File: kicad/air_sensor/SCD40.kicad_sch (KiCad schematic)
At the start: 10 parts, among them U7 ATtiny412

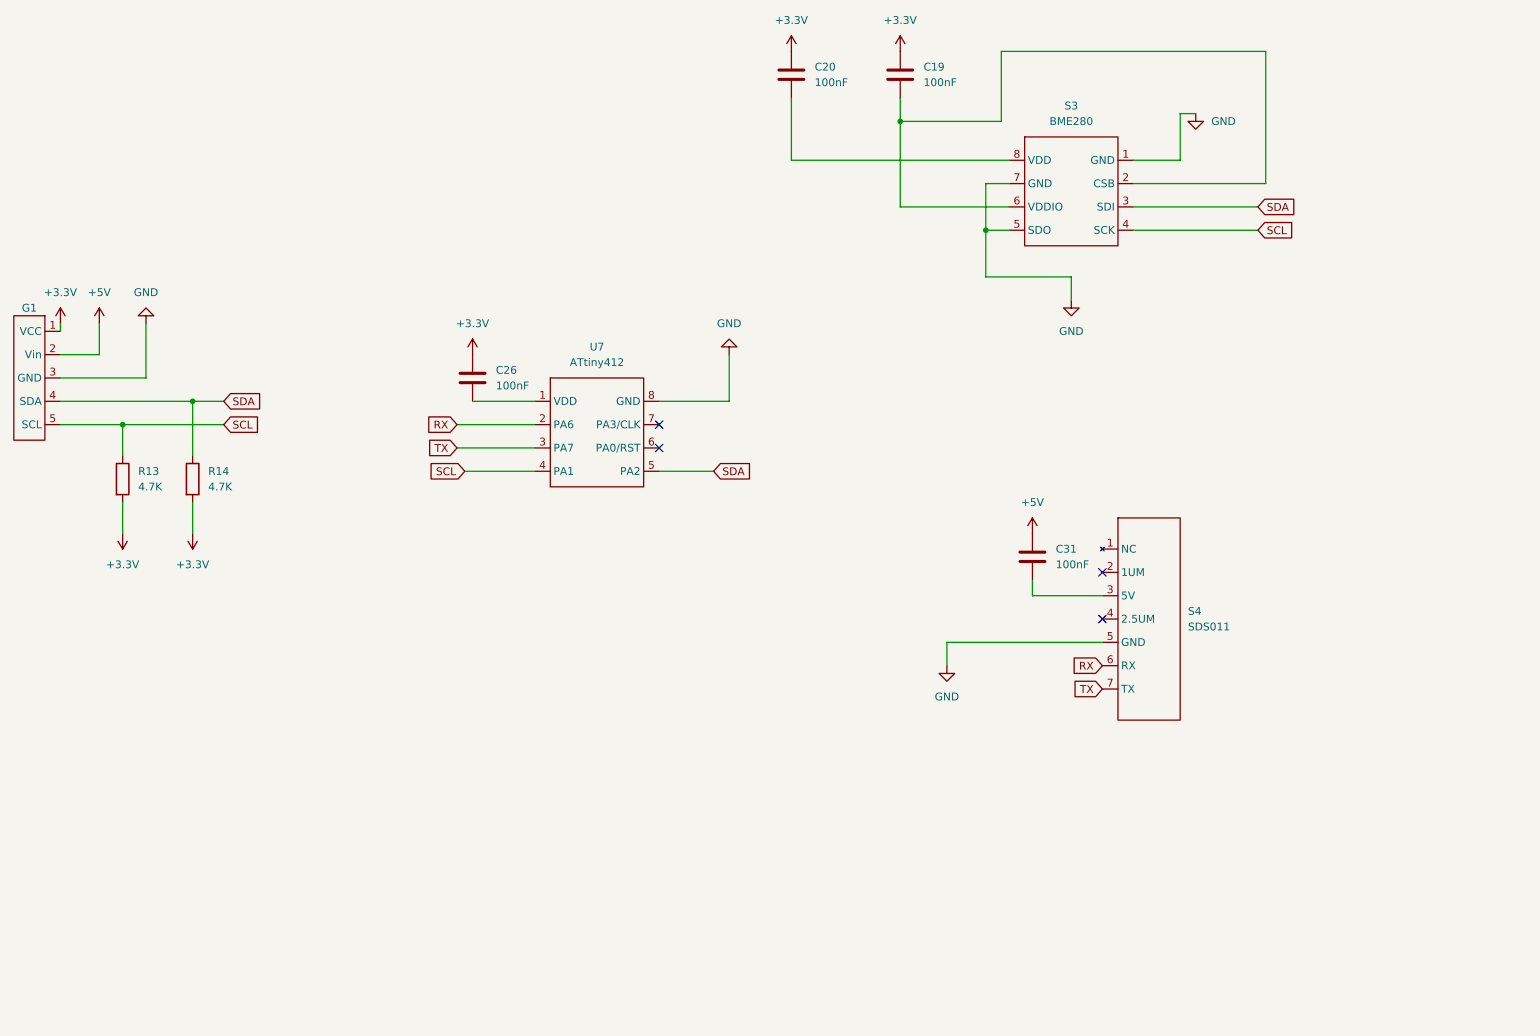
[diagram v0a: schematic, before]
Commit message: updated schema
added 5V 3A buck converter
refined 3v3 LDO
added symbols for new components
added text comments for designing the pcb
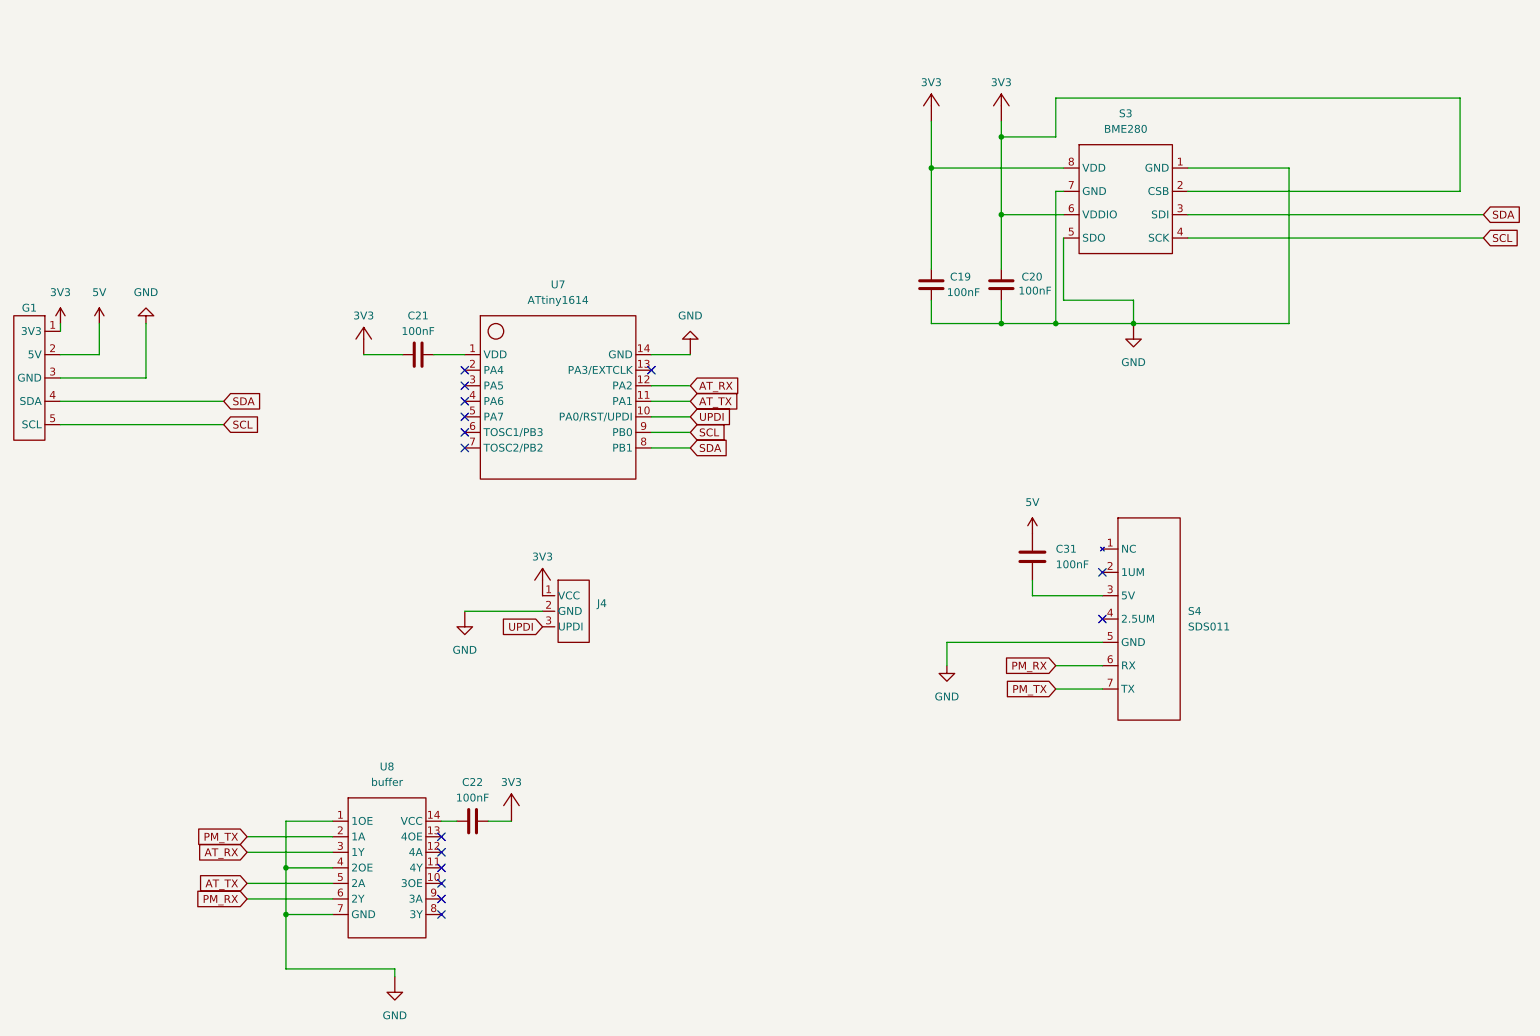
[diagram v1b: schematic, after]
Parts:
- removed C19, C20, C26: 100nF, symbol Device:C
- removed R13, R14: 4.7K, symbol Device:R
- removed U7: ATtiny412, symbol air_sens_lib:ATtiny412
- added C19, C20, C21, C22: 100nF, symbol common:Capacitor
- added J4: ~, symbol air_sens_lib:ATtiny1614_programming_header
- added U7: ATtiny1614, symbol air_sens_lib:ATtiny1614
- added U8: buffer, symbol air_sens_lib:SN74LVC125
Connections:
- net +3.3V is gone; now on net 3V3: G1.1 (3V3)
- net GND: now also C19.2, C20.1, J4.2 (GND), U7.14 (GND), U8.1 (1OE), U8.4 (2OE), U8.7 (GND)
- net SCL: now also U7.9 (PB0)
- net SDA: now also U7.8 (PB1)
- net 3V3: now reaches S3.2 (CSB), S3.6 (VDDIO)
- net 3V3: now also S3.8 (VDD), C19.1, C20.2, C21.1, C22.2, J4.1 (VCC)
- net +5V renamed 5V
- net RX renamed PM_RX
- net PM_RX: now also U8.6 (2Y)
- net TX renamed PM_TX
- net PM_TX: now also U8.2 (1A)
- new net: C22.1, U8.14 (VCC)
- new net: C21.2, U7.1 (VDD)
- new net AT_RX: U7.12 (PA2), U8.3 (1Y)
- new net AT_TX: U7.11 (PA1), U8.5 (2A)
- new net UPDI: J4.3 (UPDI), U7.10 (PA0/RST/UPDI)
- no-connect marks 4 -> 15

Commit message: updated power symbol labels, replaced power symbols in schematic with our own custom symbols
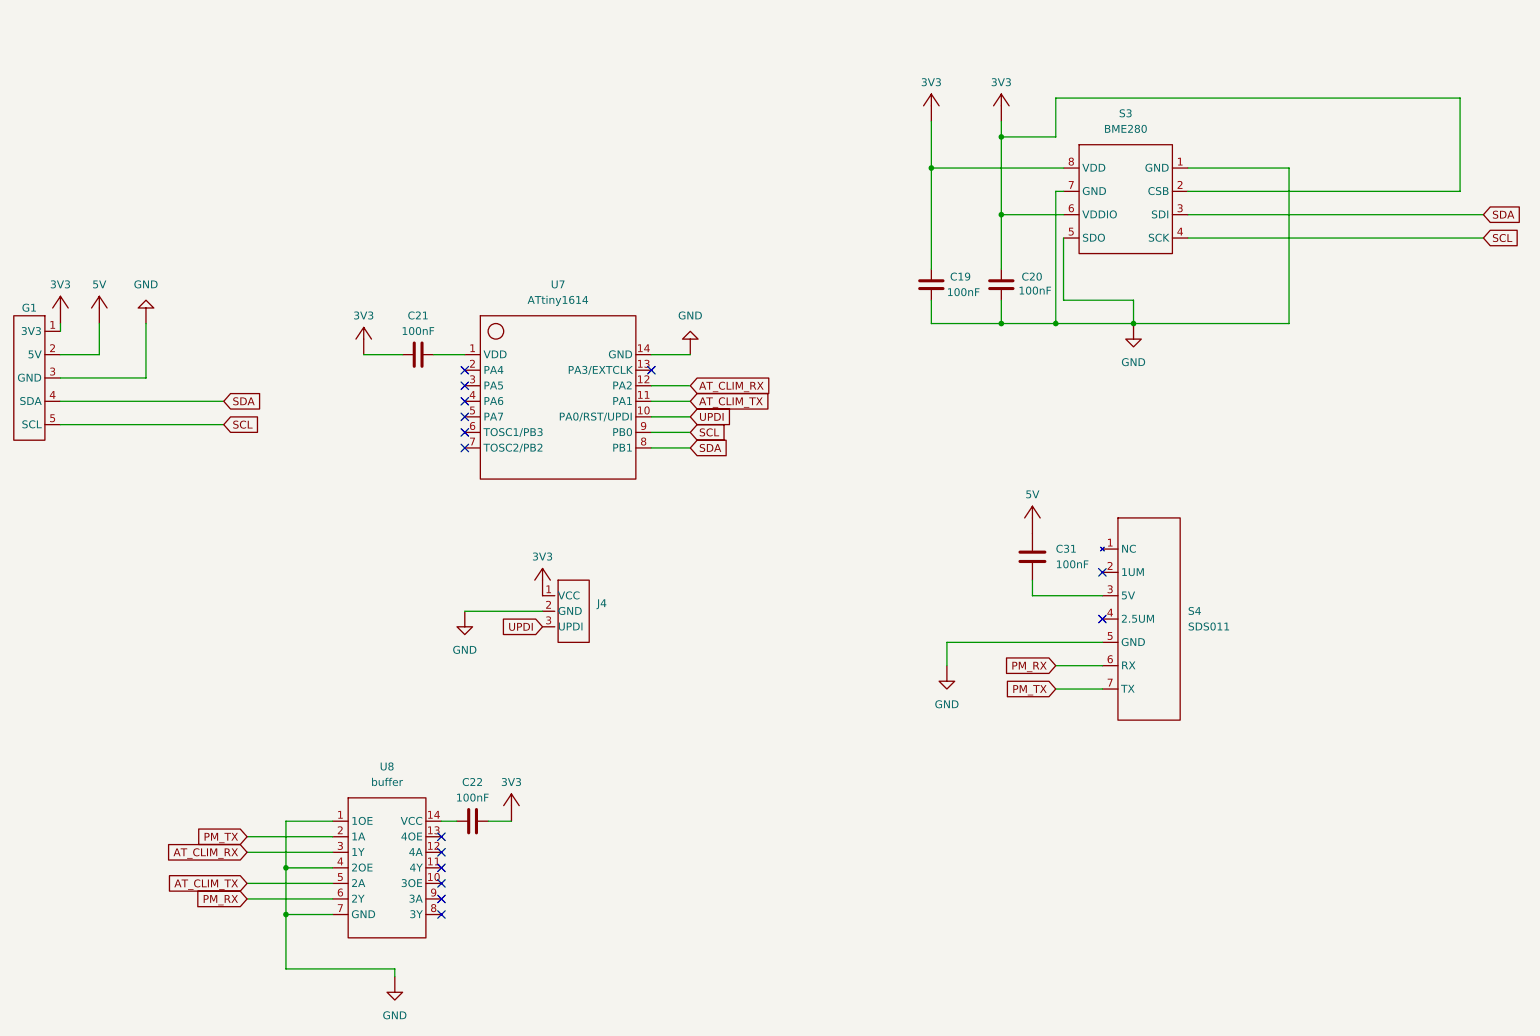
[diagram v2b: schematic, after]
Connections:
- net AT_RX renamed AT_CLIM_RX
- net AT_TX renamed AT_CLIM_TX
